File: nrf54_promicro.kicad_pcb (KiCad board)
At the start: 4 copper layers, 18 x 35 mm, 60 parts, among them J1 GSB1C4621DS1HR, J2 Conn_01x13_Socket, J3 Conn_01x13_Socket, U1 BQ24075RGT, U2 nRF54L15, U3 TPS62172DSG, U4 TPS22917DBV, Y1 32.768k, Y2 32M

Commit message: BOM Updates. Layout Updates.
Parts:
- R13: value 4.7K -> 1.5K
- R14: value 10K -> 1.5K
- moved C14 3.47 mm to (143.2, 84.0)
- moved C18 3.47 mm to (142.4, 91.0)
- moved C17 2.70 mm to (142.4, 92.4), turned to -90 degrees
- moved C13 2.60 mm to (143.2, 82.6)
- moved C12 1.83 mm to (137.6, 91.1), turned to 90 degrees
- moved C11 1.68 mm to (135.1, 92.0), turned to 180 degrees
- moved JP1 1.49 mm to (142.3, 77.0)
- moved C3 1.33 mm to (140.6, 83.6), turned to 90 degrees
- moved L2 1.09 mm to (136.5, 92.0)
- moved L1 1.09 mm to (135.4, 93.1)
- moved C22 1.05 mm to (138.8, 91.2), turned to 0 degrees
- moved L3 0.80 mm to (136.9, 91.0)
- moved C4 0.77 mm to (141.5, 84.6)
- moved C10 0.73 mm to (135.1, 94.2), turned to 180 degrees
- moved U2 0.65 mm to (136.7, 86.7)
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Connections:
- C15 pad 1: VSYS -> 5V5_VSYS
- C20 pad 1: VSYS -> 5V5_VSYS
- R12 pad 1: VSYS -> 5V5_VSYS
- R13 pad 1: VSYS -> 5V5_VSYS
- R14 pad 1: VSYS -> 5V5_VSYS
- U1 pad 10: VSYS -> 5V5_VSYS
- U1 pad 11: VSYS -> 5V5_VSYS
- U1 pad 5: GND -> 5V5_VSYS
- U1 pad 6: VSYS -> GND
- U3 pad 2: VSYS -> 5V5_VSYS
- U3 pad 3: VSYS -> 5V5_VSYS
- U4 pad 1: VSYS -> 5V5_VSYS
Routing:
- net 5V5_VSYS: track 0.00 -> 23.2 mm, vias 0 -> 6
- net VSYS: track 21.5 -> 0.00 mm, vias 5 -> 0
- net /P1.07_AIN3: track 10.8 -> 13.7 mm
- net GND: track 62.3 -> 59.6 mm, vias 76 -> 68
- net /XL1: track 3.90 -> 6.49 mm
- net /XC2: track 3.09 -> 5.22 mm
- net /P2.06: track 22.6 -> 24.5 mm
- net /P1.12_I2CSCL_AIN5: track 17.0 -> 18.9 mm
- net /VEXT_DIS_L: track 9.46 -> 11.3 mm
- net /P2.04_SPI_SDI: track 27.2 -> 28.8 mm
- net /P2.01_SPI_SCK: track 27.3 -> 28.8 mm
- net /P2.05_SPI_CS_L: track 25.9 -> 27.5 mm
- net /P2.02_SPI_SDO: track 27.2 -> 28.7 mm
- net VBAT: track 15.7 -> 14.2 mm
- net /DCC: track 1.60 -> 3.04 mm
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- added copper zone on F.Cu, net 5V5_VSYS
- added copper zone on In1.Cu, net 5V5_VSYS
- removed copper zone on F.Cu, net VSYS
- removed copper zone on In1.Cu, net VSYS
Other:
- board text added: "0.1000 mm / 0.0900 mm"
- board text added: "0.2000 mm"
- board text added: "03-05-2025"
- board text added: "1.1382 mm"
- board text added: "18.0000 mm x 35.0000 mm"
- board text added: "Layout Changes"
- board text added: "USB-C"
- board text removed: "0.10 mm / 0.09 mm"
- board text removed: "0.20 mm"
- board text removed: "1.20 mm"
- board text removed: "18.00 mm x 35.00 mm"
- board text removed: "7628"

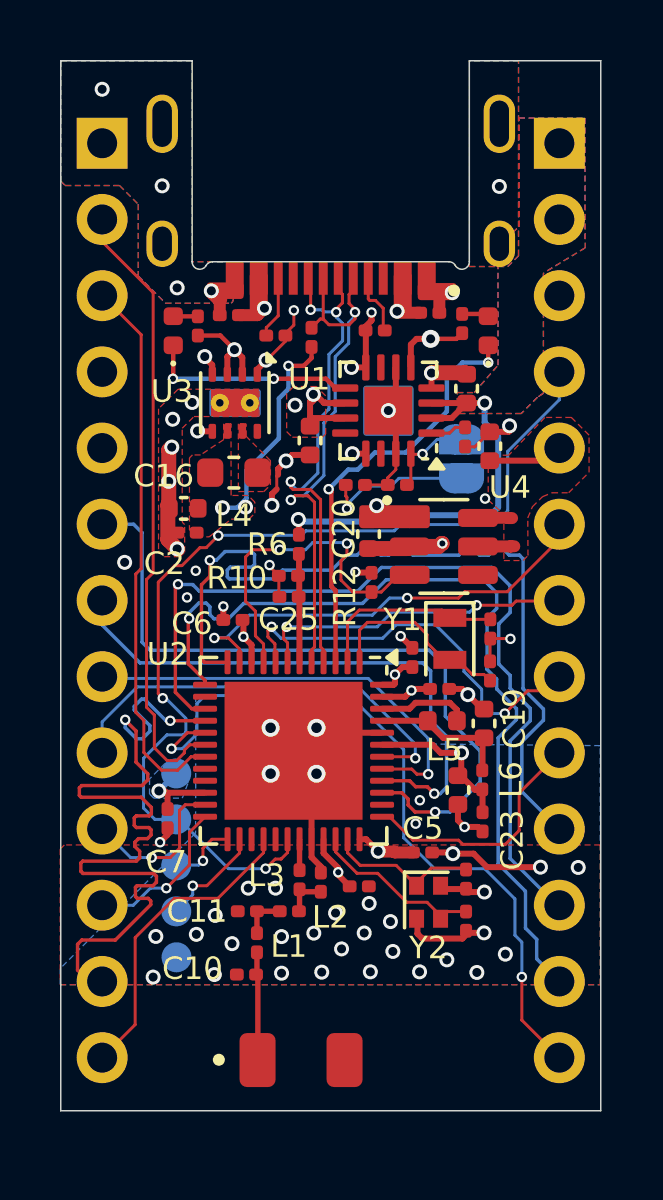
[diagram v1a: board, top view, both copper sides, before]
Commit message: Moved USB_D_P/N to MCU Domain for increased bus BW. Improved RF layout. Improved PI. Changed IO for improved MCU escape.
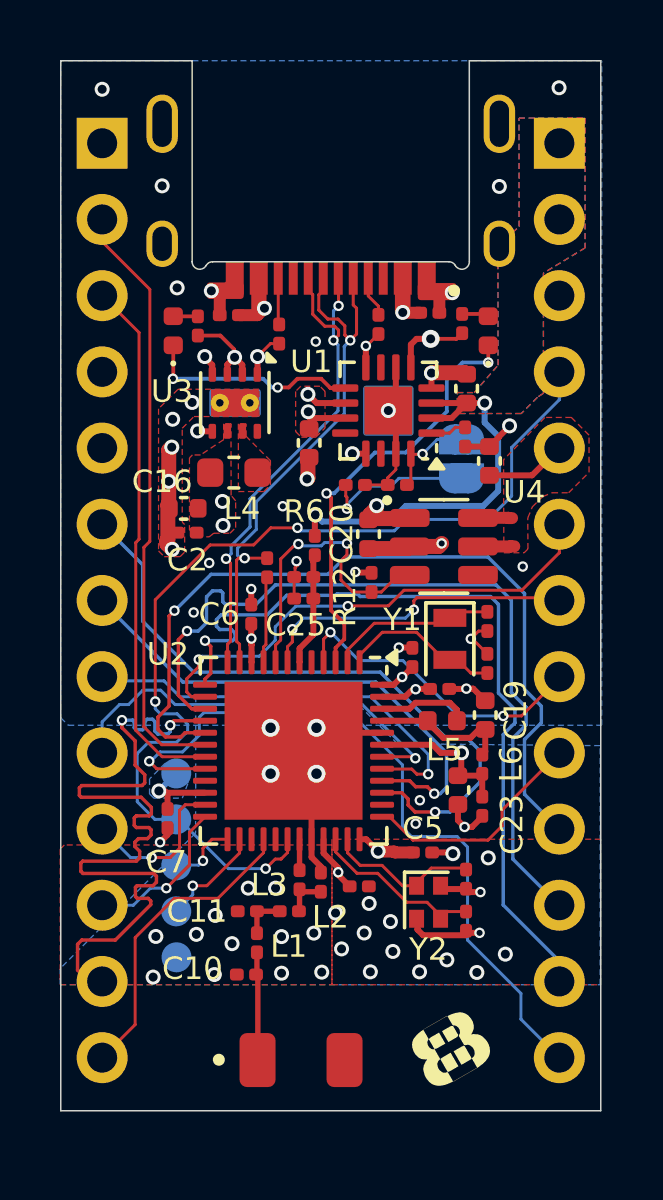
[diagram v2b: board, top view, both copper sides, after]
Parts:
- moved R1 7.82 mm to (135.8, 80.6)
- moved C6 0.64 mm to (135.2, 82.2), turned to 90 degrees
- moved R6 0.53 mm to (137.4, 79.9)
- moved C23 0.52 mm to (142.9, 88.5)
- moved L6 0.52 mm to (142.9, 87.2)
- moved R10 0.51 mm to (137.0, 80.9)
- moved C25 0.49 mm to (137.0, 81.6)
- moved C21 0.49 mm to (143.2, 77.0)
- moved C19 0.28 mm to (143.1, 85.5)
- moved C13 0.27 mm to (143.1, 82.4)
- moved C14 0.27 mm to (143.1, 83.8)
- moved R4 0.23 mm to (139.5, 72.5), turned to -90 degrees
- moved R5 0.12 mm to (136.2, 72.8), turned to -90 degrees
- moved C15 0.09 mm to (137.2, 76.4)
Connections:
- J3 pad 10: /P2.01_SPI_SCK -> /P2.06_SPI_SCK
- J3 pad 13: /P2.06 -> /P2.09
- J3 pad 6: /P2.00 -> /P2.03
- J3 pad 8: /P1.07_AIN3 -> /P1.03
- R1 pad 1: 3V3_VCC -> /USB_DRV
- U2 pad 11: /P2.00 -> /USB_D_N
- U2 pad 12: /P2.01_SPI_SCK -> /USB_D_P
- U2 pad 14: unconnected-(U2-P2.03-Pad14) -> /P2.03
- U2 pad 17: /P2.06 -> /P2.06_SPI_SCK
- U2 pad 20: unconnected-(U2-P2.09-Pad20) -> /P2.09
- U2 pad 4: /USB_D_P -> /P1.03
- U2 pad 5: /USB_D_N -> unconnected-(U2-P1.04-Pad5)
- U2 pad 8: /P1.07_AIN3 -> /VEXT_DIS_L
- U2 pad 9: /VEXT_DIS_L -> /USB_DRV
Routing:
- net /P2.01_SPI_SCK: track 28.8 -> 0.00 mm, vias 1 -> 0
- net /P2.06_SPI_SCK: track 0.00 -> 27.6 mm, vias 0 -> 1
- net /P2.09: track 0.00 -> 25.0 mm, vias 0 -> 1
- net /P2.06: track 24.5 -> 0.00 mm, vias 2 -> 0
- net /P2.03: track 0.00 -> 16.6 mm, vias 0 -> 2
- net /P2.00: track 14.8 -> 0.00 mm, vias 2 -> 0
- net /P1.07_AIN3: track 13.7 -> 0.00 mm, vias 2 -> 0
- net /P1.03: track 0.00 -> 10.5 mm, vias 0 -> 2
- net GND: track 59.6 -> 49.9 mm, vias 68 -> 66
- net 3V3_VCC: track 17.1 -> 9.39 mm, vias 8 -> 7
- net /USB_DRV: track 0.00 -> 2.88 mm
- net /P1.11_I2CSDA_AIN4: track 23.9 -> 21.9 mm
- net /P1.12_I2CSCL_AIN5: track 18.9 -> 17.2 mm
- net /P2.04_SPI_SDI: track 28.8 -> 27.2 mm
- net /VEXT_DIS_L: track 11.3 -> 9.95 mm
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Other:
- board text added: "03-10-2025"
- board text added: "STACKUP"
- board text removed: "03-05-2025"

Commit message: Fixed Assembly Layers.
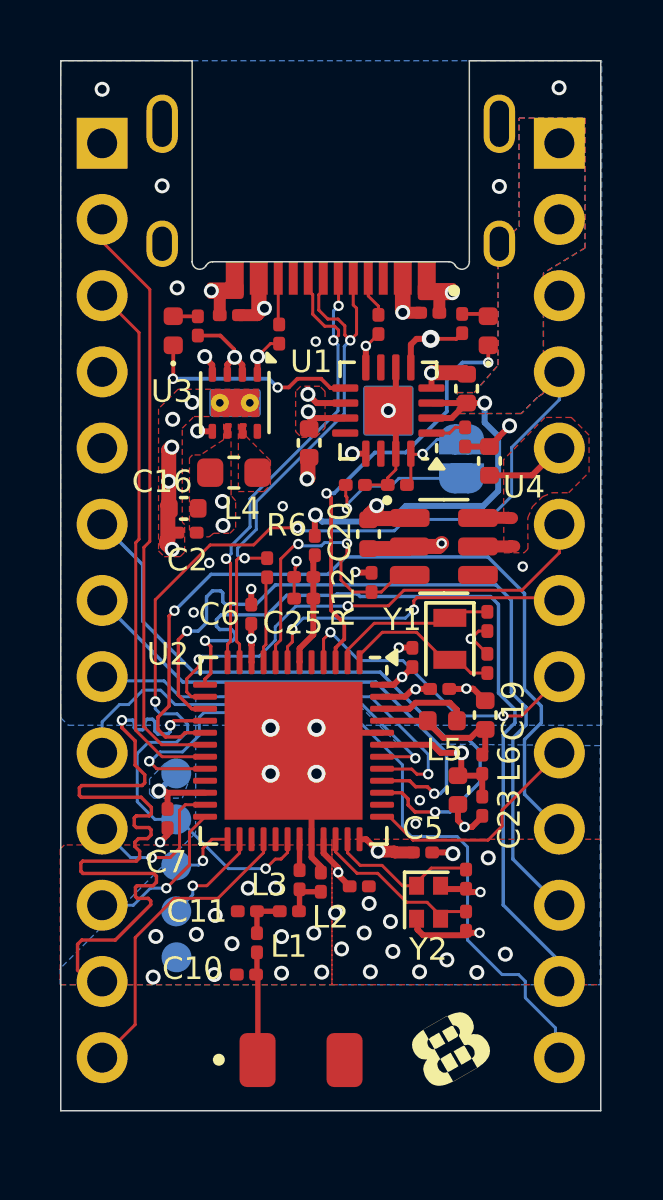
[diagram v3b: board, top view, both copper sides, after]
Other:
- board text added: "03-12-2025"
- board text added: "IMPEDANCE TABLE"
- board text removed: "03-10-2025"

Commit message: Modified layout - remove SPI LM. Removed GND shape around pins.
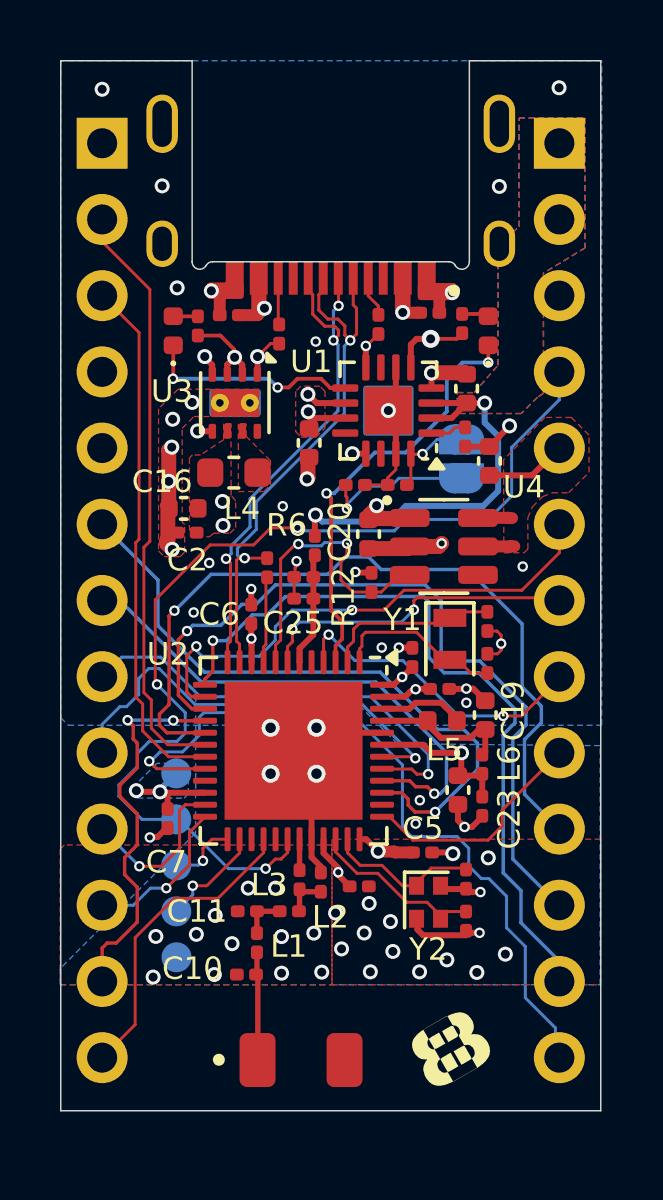
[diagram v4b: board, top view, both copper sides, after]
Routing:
- net /P2.05_SPI_CS_L: track 26.3 -> 12.9 mm
- net /P2.02_SPI_SDO: track 27.4 -> 24.9 mm
- net /P2.04_SPI_SDI: track 27.2 -> 25.4 mm
- net /P2.06_SPI_SCK: track 27.6 -> 26.7 mm
- net /P1.14_TIMR10_AIN7: track 14.0 -> 14.9 mm
- net 3V3_VCC: track 9.39 -> 10.1 mm, vias 7 -> 8
- net /P2.03: track 16.6 -> 17.3 mm
- net /P1.13_TIMR10_AIN6: track 14.2 -> 14.8 mm
- net GND: track 49.9 -> 50.2 mm, vias 66 -> 68
